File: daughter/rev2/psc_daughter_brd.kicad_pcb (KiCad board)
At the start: 10 copper layers, 40 x 160 mm, 343 parts, among them J1 61082-061400LF, J2 61082-061400LF, U1 AD8221, U10 BUF634AIDR, U11 BUF634AIDR, U12 ADR1001AEZ, U13 ADS8568SPM, U14 AD8221, U15 OPA277, U16 AD8221, U17 OPA277, U18 AD8221, U19 OPA277, U2 OPA277, U20 LT3042xMSE, U21 THP210DR, U22 LT6202CS5, U23 ADA4523-1BRMZ, U24 LT6202CS5, U26 THP210DR, U27 AD8429BRZ, U3 AD8676ARZ, U31 LTC2376CDE-20, U32 LTC6655BHLS8-5, U33 AD8429BRZ, U35 LT6202CS5, U37 LTC2376CDE-20, U38 TXUN0104RUTR, U39 ADUM5240ARZ, U4 AD8676xR, U40 ADUM5240ARZ, U41 TXUN0104RUTR, U42 ADUM5242ARZ, U43 ADUM5242ARZ, U5 AD5791BRUZ, U6 AD797ARZ, U7 OPA277, U8 AD8676xR, U9 OPA277

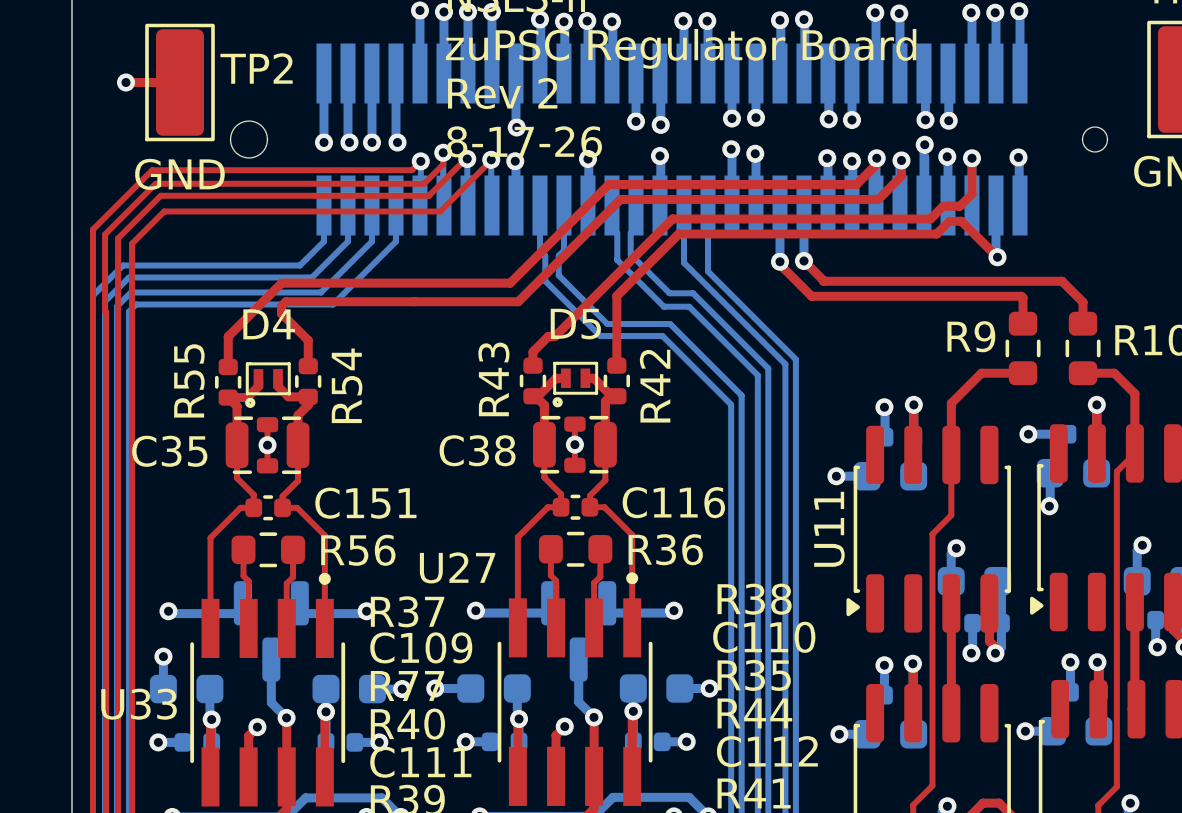
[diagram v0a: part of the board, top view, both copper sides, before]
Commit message: Add parallel resistor for AD8429 gain to be exactly 10
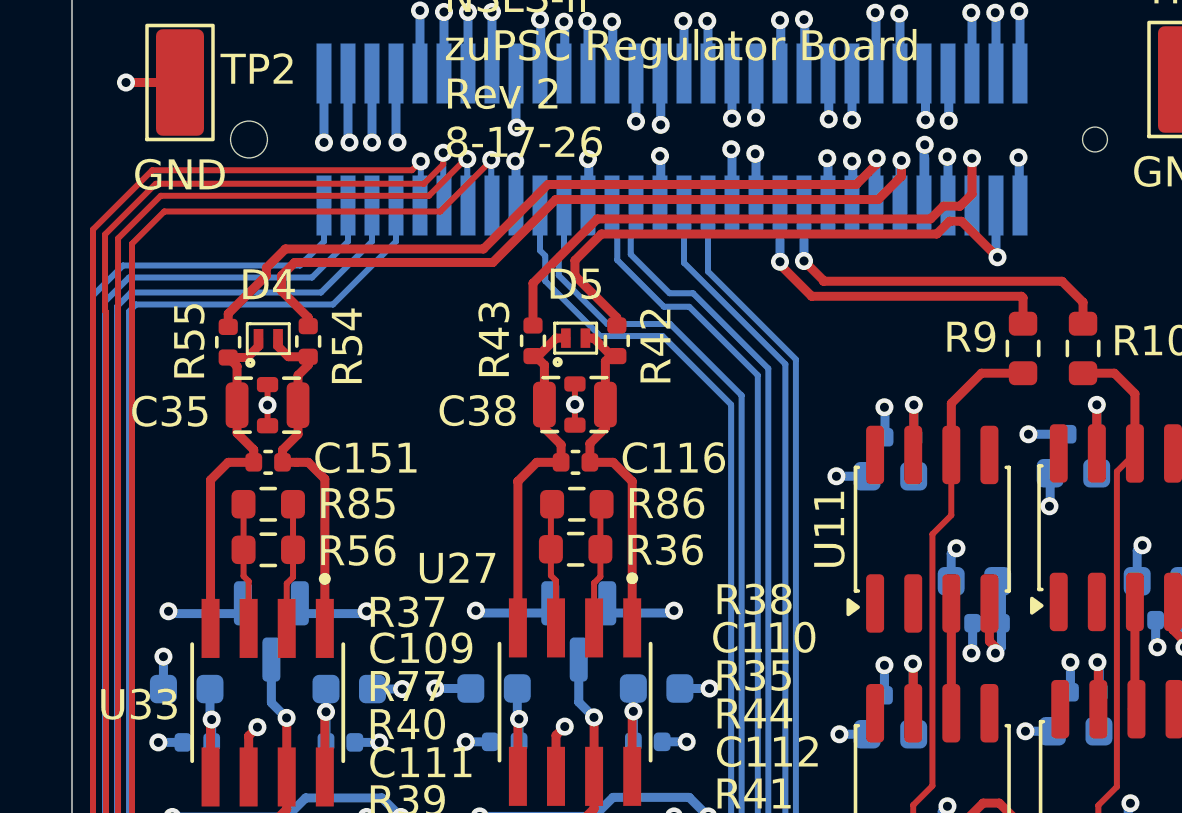
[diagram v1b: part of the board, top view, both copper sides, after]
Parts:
- added R85: 665, Resistor_SMD:R_0603_1608Metric, F.Cu at (146.5, 59.2)
- added R86: 665, Resistor_SMD:R_0603_1608Metric, F.Cu at (156.8, 59.2)
- moved C151 1.52 mm to (146.5, 57.8)
- moved C116 1.50 mm to (156.8, 57.8)
- moved C38 1.34 mm to (156.8, 55.8)
- moved D5 1.34 mm to (156.8, 53.6)
- moved R42 1.34 mm to (158.2, 53.7)
- moved R43 1.34 mm to (155.4, 53.7)
- moved C35 1.34 mm to (146.5, 55.9)
- moved R54 1.34 mm to (147.9, 53.7)
- moved R55 1.34 mm to (145.2, 53.8)
- moved D4 1.34 mm to (146.5, 53.6)
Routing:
- net Net-(D4-A1): track 10.3 -> 11.9 mm
- net Net-(D5-A1): track 10.4 -> 11.9 mm
- net Net-(D4-A2): track 10.3 -> 11.9 mm
- net Net-(R56-Pad2): track 2.69 -> 4.21 mm
- net Net-(R56-Pad1): track 2.71 -> 4.23 mm
- net Net-(R36-Pad1): track 2.71 -> 4.22 mm
- net Net-(R36-Pad2): track 2.69 -> 4.21 mm
- net Net-(D5-A2): track 10.4 -> 11.9 mm
- net /DCCT ADCs/dcct1-: track 18.3 -> 19.6 mm
- net /DCCT ADCs/dcct0-: track 26.9 -> 26.1 mm
- net /DCCT ADCs/dcct0+: track 26.8 -> 26.1 mm
